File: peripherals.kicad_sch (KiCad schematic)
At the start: 84 parts, among them J14 CONMMCX002-SMD-T, J5 U_FL-R-SMT-1_10_, J7 DM3AT-SF-PEJM5, J8 693022010811, Q13 BSS138-7-F, Q15 BSS138-7-F, Q8 BSS138-7-F, U10 NCP163ASN330T1G

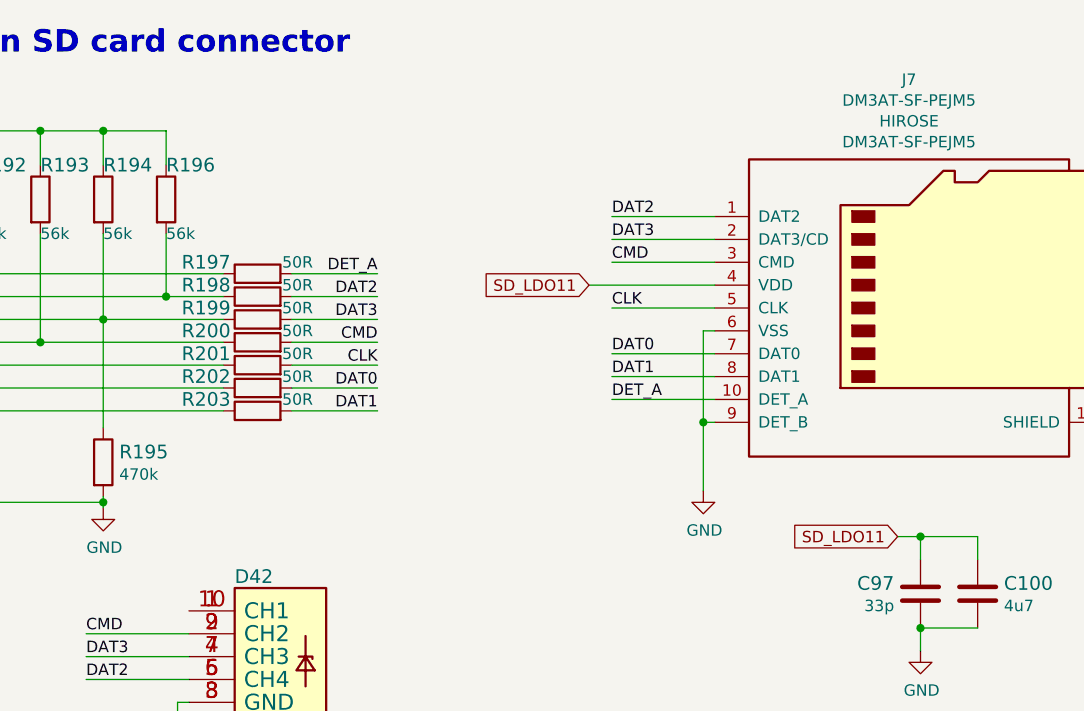
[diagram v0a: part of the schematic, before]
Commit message: Cleared old files. Added 0R after DCDC converters
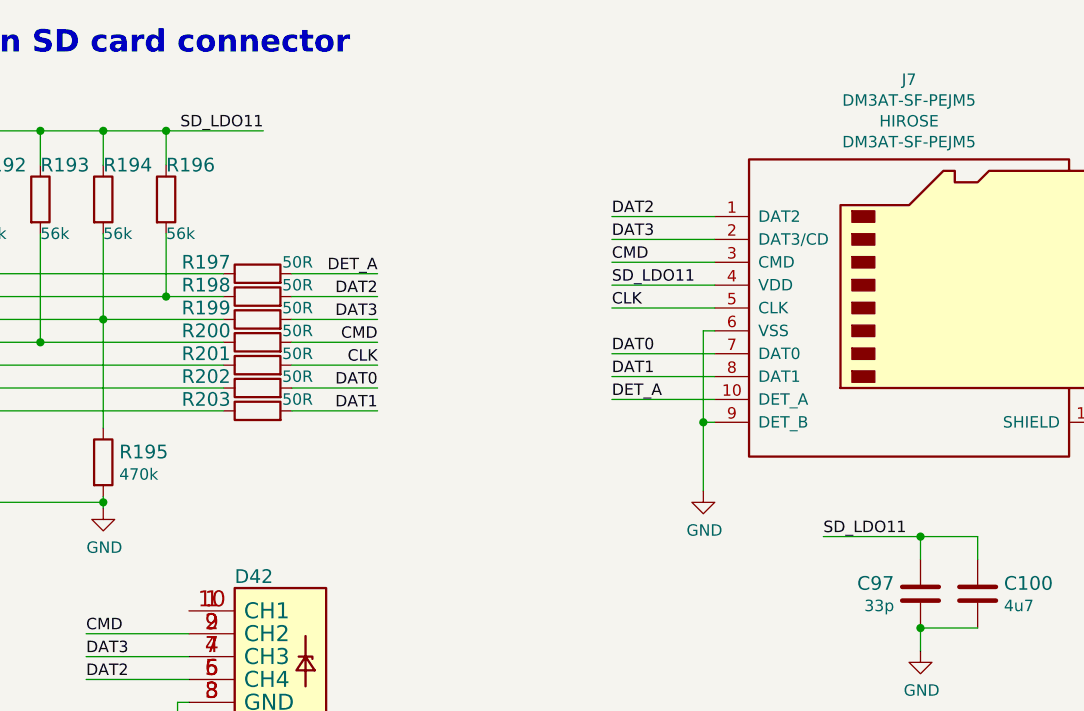
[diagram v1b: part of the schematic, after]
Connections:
- net SD_LDO11 is gone; now on net SD.LDO11: C100.1, C97.1, J7.4 (VDD)

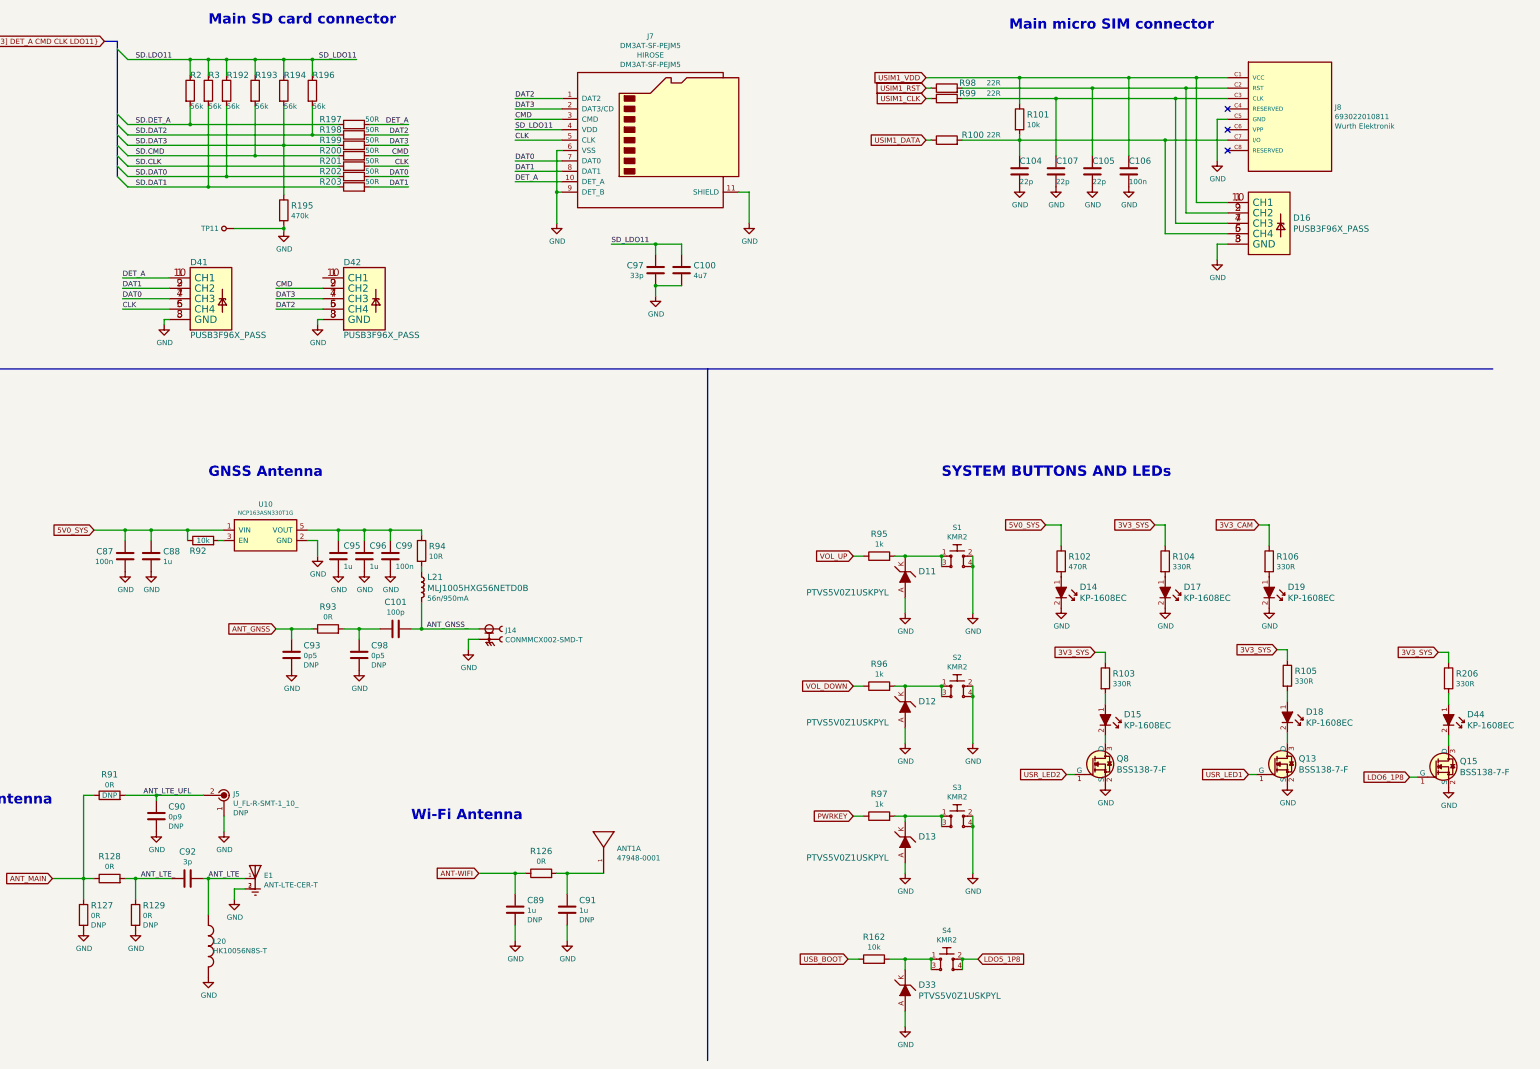
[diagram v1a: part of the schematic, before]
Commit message: Introduce component standardization
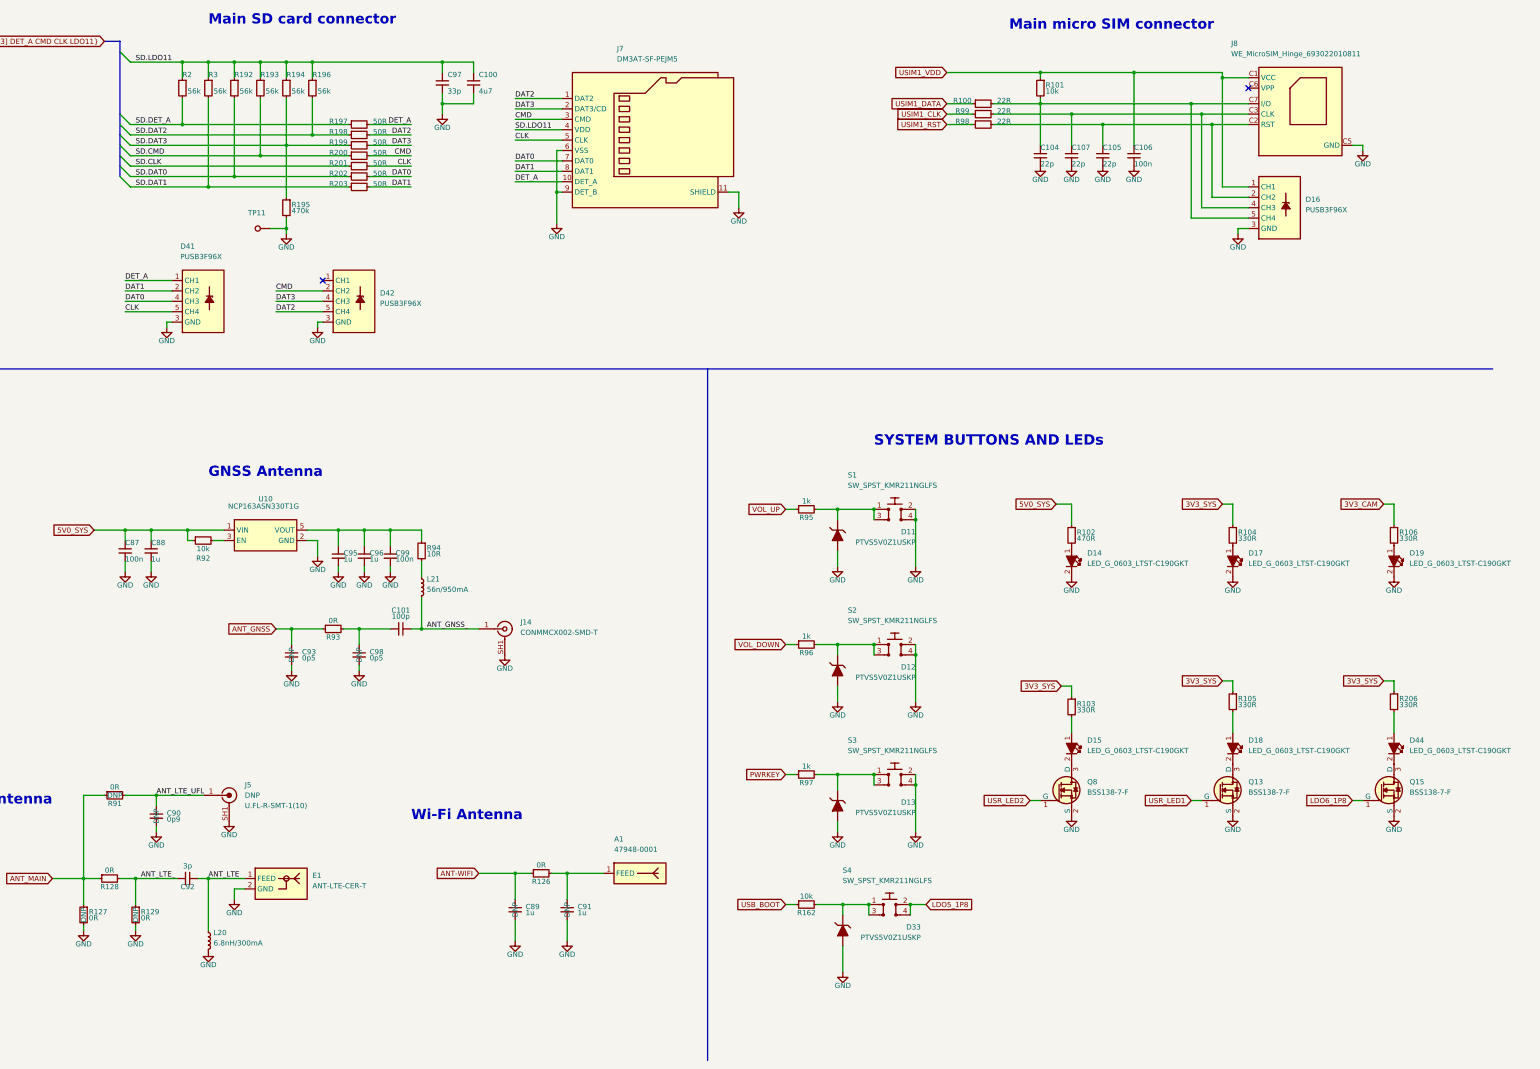
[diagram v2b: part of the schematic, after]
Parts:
- A1: renamed from ANT1; symbol sc606-baseboard:47948-0001-antmicroRFAntennas -> sc606-baseboard:47948-0001; Author (none) -> Antmicro; License (none) -> Apache-2.0
- C100: footprint sc606-baseboard-footprints:0402-cap -> sc606-baseboard-footprints:C_0402_1005Metric; Author (none) -> Antmicro; License (none) -> Apache-2.0; Manufacturer MURATA -> Murata
- C101: footprint sc606-baseboard-footprints:0402-cap -> sc606-baseboard-footprints:C_0402_1005Metric; Author (none) -> Antmicro; Dielectric (none) -> C0G; License (none) -> Apache-2.0; MPN 0402N101J500CT -> GCM1555C1H101JA16D; Manufacturer WALSIN -> Murata; Voltage (none) -> 50V
- C104, C105, C107: footprint sc606-baseboard-footprints:0402-cap -> sc606-baseboard-footprints:C_0402_1005Metric; Author (none) -> Antmicro; License (none) -> Apache-2.0; Manufacturer YAGEO -> Yaego
- C106: footprint sc606-baseboard-footprints:0402-cap -> sc606-baseboard-footprints:C_0402_1005Metric; Author (none) -> Antmicro; Dielectric (none) -> X5R; License (none) -> Apache-2.0; MPN 0402X104K6R3CT -> GRM155R61H104KE14D; Manufacturer Walsin -> Murata; Voltage (none) -> 50V
- C87, C99: footprint sc606-baseboard-footprints:0402-cap -> sc606-baseboard-footprints:C_0402_1005Metric; Author (none) -> Antmicro; Dielectric (none) -> X5R; License (none) -> Apache-2.0; Voltage (none) -> 50V
- C88, C89, C91, C95, C96: footprint sc606-baseboard-footprints:0402-cap -> sc606-baseboard-footprints:C_0402_1005Metric; Author (none) -> Antmicro; License (none) -> Apache-2.0
- C90: footprint sc606-baseboard-footprints:0402-cap -> sc606-baseboard-footprints:C_0402_1005Metric; Author (none) -> Antmicro; License (none) -> Apache-2.0; MPN GJM1555C1HR90DB01D -> GJM1555C1HR90DB01D; Manufacturer MURATA -> Murata
- C92, C97: footprint sc606-baseboard-footprints:0402-cap -> sc606-baseboard-footprints:C_0402_1005Metric; Author (none) -> Antmicro; License (none) -> Apache-2.0; Manufacturer MULTICOMP -> Multicomp
- C93, C98: footprint sc606-baseboard-footprints:0402-cap -> sc606-baseboard-footprints:C_0402_1005Metric; Author (none) -> Antmicro; License (none) -> Apache-2.0; MPN GJM1555C1HR50WB01D -> GJM1555C1HR50WB01D; Manufacturer MURATA -> Murata
- D11, D12, D13, D33: value PTVS5V0Z1USKPYL -> PTVS5V0Z1USKP; symbol sc606-baseboard:PTVS5V0Z1USKPYL -> sc606-baseboard:PTVS5V0Z1USKP; Author (none) -> Antmicro; License (none) -> Apache-2.0
- D14, D15, D17, D18, D19, D44: value KP-1608EC -> LED_G_0603_LTST-C190GKT; footprint sc606-baseboard-footprints:LED_0603 -> sc606-baseboard-footprints:LED_0603_1608Metric_G; symbol sc606-baseboard:KP-1608EC -> sc606-baseboard:LED_G_0603_LTST-C190GKT; Author (none) -> Antmicro; License (none) -> Apache-2.0; MPN KP-1608EC -> LTST-C190GKT; Manufacturer KINGBRIGHT -> Lite-On Inc.
- D16, D41, D42: footprint sc606-baseboard-footprints:PUSB3F96X -> sc606-baseboard-footprints:Nexperia_DFN-10_2.5x1mm_P0.5mm; Author (none) -> Antmicro; License (none) -> Apache-2.0
- E1: footprint sc606-baseboard-footprints:XDCR_ANT-LTE-CER-T -> sc606-baseboard-footprints:Antenna_ANT-LTE-CER-T; Author (none) -> Antmicro; License (none) -> Apache-2.0
- J14: Author (none) -> Antmicro; License (none) -> Apache-2.0; MANUFACTURER Linx Technologies -> (none); Manufacturer (none) -> Linx
- J5: value U_FL-R-SMT-1_10_ -> U_FL-R-SMT-1; symbol sc606-baseboard:U_FL-R-SMT-1_10_ -> sc606-baseboard:U_FL-R-SMT-1; Author (none) -> Antmicro; License (none) -> Apache-2.0; Manufacturer Hirose Electric Co Ltd -> Hirose
- J7: Author (none) -> Antmicro; License (none) -> Apache-2.0; Manufacturer HIROSE -> Hirose
- J8: value 693022010811 -> WE_MicroSIM_Hinge_693022010811; symbol sc606-baseboard:693022010811 -> sc606-baseboard:WE_MicroSIM_Hinge_693022010811; Author (none) -> Antmicro; License (none) -> Apache-2.0; Manufacturer Wurth Elektronik -> Würth Elektronik
- L20: Author (none) -> Antmicro; License (none) -> Apache-2.0; Val (none) -> 6.8nH/300mA
- L21: footprint sc606-baseboard-footprints:0402-res -> sc606-baseboard-footprints:L_0402_1005Metric; Author (none) -> Antmicro; License (none) -> Apache-2.0; MaxCur 950mA -> (none)
- Q13, Q15, Q8: Author (none) -> Antmicro; License (none) -> Apache-2.0
- R100, R98, R99: footprint sc606-baseboard-footprints:0402-res -> sc606-baseboard-footprints:R_0402_1005Metric; Author (none) -> Antmicro; License (none) -> Apache-2.0; MPN CRCW040222R0FKED -> CR0402-FX-22R0GLF; Manufacturer VISHAY -> Bourns; Tolerance (none) -> 1%
- R101, R162, R92: footprint sc606-baseboard-footprints:0402-res -> sc606-baseboard-footprints:R_0402_1005Metric; Author (none) -> Antmicro; License (none) -> Apache-2.0; MPN CRCW040210K0FKEDHP -> CR0402-FX-1002GLF; Manufacturer VISHAY -> Bourns; Tolerance (none) -> 1%
- R102: footprint sc606-baseboard-footprints:0402-res -> sc606-baseboard-footprints:R_0402_1005Metric; Author (none) -> Antmicro; License (none) -> Apache-2.0; MPN CRCW0402470RFKED -> CR0402-FX-4700GLF; Manufacturer VISHAY -> Bourns; Tolerance (none) -> 1%
- R103, R104, R105, R106, R206: footprint sc606-baseboard-footprints:0402-res -> sc606-baseboard-footprints:R_0402_1005Metric; Author (none) -> Antmicro; License (none) -> Apache-2.0; MPN MCMR04X3300FTL -> CR0402-FX-3300GLF; Manufacturer MULTICOMP -> Bourns; Tolerance (none) -> 1%
- R126, R127, R128, R129, R91, R93: footprint sc606-baseboard-footprints:0402-res -> sc606-baseboard-footprints:R_0402_1005Metric; Author (none) -> Antmicro; Current (none) -> 1A; License (none) -> Apache-2.0; Manufacturer PANASONIC -> Panasonic
- R192, R193, R194, R196, R2, R3: footprint sc606-baseboard-footprints:0402-res -> sc606-baseboard-footprints:R_0402_1005Metric; Author (none) -> Antmicro; License (none) -> Apache-2.0; MPN CRCW040256K0FKED -> CR0402-FX-5602GLF; Manufacturer VISHAY -> Bourns; Tolerance (none) -> 1%
- R195: footprint antmicro-footprints:0402-res -> sc606-baseboard-footprints:R_0402_1005Metric; symbol antmicroResistors0402:R_470k_0402 -> sc606-baseboard:R_470k_0402; Author (none) -> Antmicro; License (none) -> Apache-2.0; MPN RC0402FR-07470KL -> CR0402-FX-4703GLF; Manufacturer YAGEO -> Bourns; Tolerance (none) -> 1%
- R197, R198, R199, R200, R201, R202, R203: footprint sc606-baseboard-footprints:0402-res -> sc606-baseboard-footprints:R_0402_1005Metric; Author (none) -> Antmicro; License (none) -> Apache-2.0; MPN RN73R1ETTP50R0F50 -> CR0402-FX-50R0GLF; Manufacturer KOA -> Bourns; Tolerance (none) -> 1%
- R94: footprint sc606-baseboard-footprints:0603-res -> sc606-baseboard-footprints:R_0603_1608Metric; Author (none) -> Antmicro; License (none) -> Apache-2.0; MPN MCWR06X10R0FTL -> CR0603-FX-10R0ELF; Manufacturer MULTICOMP -> Bourns; Tolerance (none) -> 1%
- R95, R96, R97: footprint sc606-baseboard-footprints:0402-res -> sc606-baseboard-footprints:R_0402_1005Metric; Author (none) -> Antmicro; License (none) -> Apache-2.0; Manufacturer BOURNS -> Bourns; Tolerance (none) -> 1%
- S1, S2, S3, S4: value KMR2 -> SW_SPST_KMR211NGLFS; symbol sc606-baseboard:KMR2 -> sc606-baseboard:SW_SPST_KMR211NGLFS; Author (none) -> Antmicro; License (none) -> Apache-2.0; Manufacturer C&K Components -> C&K
- TP11: value TP_SMD_1_5MM -> TP_1.5mm_SMD; footprint sc606-baseboard-footprints:TP-R-1.5 -> sc606-baseboard-footprints:TP_SMD_1.5mm; symbol sc606-baseboard:TP_SMD_0_75MM -> sc606-baseboard:TP_1.5mm_SMD; Author (none) -> Antmicro; License (none) -> Apache-2.0
- U10: Author (none) -> Antmicro; License (none) -> Apache-2.0; Manufacturer Onsemi -> ON Semiconductor
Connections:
- net ANT_LTE_UFL: now also J5.1; no longer J5.2
- net GND: now also J14.SH1, J14.SH2, J14.SH3, J14.SH4, J5.SH1, J5.SH2; no longer J14.S1, J14.S2, J14.S3, J14.S4, J5.1
- no-connect marks 3 -> 2
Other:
- moved on the sheet: C100, C101, C104, C105, C106, C107, C87, C88, C89, C90, C91, C92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

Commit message: [#61796] Run globlib
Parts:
- A1: footprint sc606-baseboard-footprints:47948-0001 -> antmicro-footprints:47948-0001; symbol sc606-baseboard:47948-0001 -> antmicroRFAntennas:47948-0001
- C100: footprint sc606-baseboard-footprints:C_0402_1005Metric -> antmicro-footprints:C_0402_1005Metric; symbol sc606-baseboard:C_4u7_0402 -> antmicroCapacitors0402:C_4u7_0402
- C101: footprint sc606-baseboard-footprints:C_0402_1005Metric -> antmicro-footprints:C_0402_1005Metric; symbol sc606-baseboard:C_100p_0402 -> antmicroCapacitors0402:C_100p_0402
- C104, C105, C107: footprint sc606-baseboard-footprints:C_0402_1005Metric -> antmicro-footprints:C_0402_1005Metric; symbol sc606-baseboard:C_22p_0402 -> antmicroCapacitors0402:C_22p_0402
- C106, C87, C99: footprint sc606-baseboard-footprints:C_0402_1005Metric -> antmicro-footprints:C_0402_1005Metric; symbol sc606-baseboard:C_100n_0402 -> antmicroCapacitors0402:C_100n_0402
- C88, C89, C91, C95, C96: footprint sc606-baseboard-footprints:C_0402_1005Metric -> antmicro-footprints:C_0402_1005Metric; symbol sc606-baseboard:C_1u_0402 -> antmicroCapacitors0402:C_1u_0402
- C90: footprint sc606-baseboard-footprints:C_0402_1005Metric -> antmicro-footprints:C_0402_1005Metric; symbol sc606-baseboard:C_0p9_0402 -> antmicroCapacitors0402:C_0p9_0402
- C92: footprint sc606-baseboard-footprints:C_0402_1005Metric -> antmicro-footprints:C_0402_1005Metric; symbol sc606-baseboard:C_3p_0402 -> antmicroCapacitors0402:C_3p_0402
- C93, C98: footprint sc606-baseboard-footprints:C_0402_1005Metric -> antmicro-footprints:C_0402_1005Metric; symbol sc606-baseboard:C_0p5_0402 -> antmicroCapacitors0402:C_0p5_0402
- C97: footprint sc606-baseboard-footprints:C_0402_1005Metric -> antmicro-footprints:C_0402_1005Metric; symbol sc606-baseboard:C_33p_0402 -> antmicroCapacitors0402:C_33p_0402
- D11, D12, D13, D33: footprint sc606-baseboard-footprints:SOD-964 -> antmicro-footprints:D_SOD-964; symbol sc606-baseboard:PTVS5V0Z1USKP -> antmicroTVSDiodes:PTVS5V0Z1USKP
- D14, D15, D17, D18, D19, D44: footprint sc606-baseboard-footprints:LED_0603_1608Metric_G -> antmicro-footprints:LED_0603_1608Metric_G; symbol sc606-baseboard:LED_G_0603_LTST-C190GKT -> antmicroLEDIndicationDiscrete:LED_G_0603_LTST-C190GKT
- D16, D41, D42: footprint sc606-baseboard-footprints:Nexperia_DFN-10_2.5x1mm_P0.5mm -> antmicro-footprints:Nexperia_DFN-10_2.5x1mm_P0.5mm; symbol sc606-baseboard:PUSB3F96X_PASS -> antmicroTVSDiodes:PUSB3F96X_PASS
- E1: footprint sc606-baseboard-footprints:Antenna_ANT-LTE-CER-T -> antmicro-footprints:Antenna_ANT-LTE-CER-T; symbol sc606-baseboard:ANT-LTE-CER-T -> antmicroRFAntennas:ANT-LTE-CER-T
- J14: footprint sc606-baseboard-footprints:LINX_CONMMCX002-SMD-T -> antmicro-footprints:LINX_CONMMCX002-SMD-T; symbol sc606-baseboard:CONMMCX002-SMD-T -> antmicroCoaxialConnectorsRF:CONMMCX002-SMD-T
- J5: footprint sc606-baseboard-footprints:Coax_Conn_U.FL -> antmicro-footprints:Coax_Conn_U.FL; symbol sc606-baseboard:U_FL-R-SMT-1 -> antmicroCoaxialConnectorsRF:U_FL-R-SMT-1
- J7: footprint sc606-baseboard-footprints:MicroSD_DM3AT-SF-PEJM5 -> antmicro-footprints:MicroSD_DM3AT-SF-PEJM5; symbol sc606-baseboard:DM3AT-SF-PEJM5 -> antmicroMemoryConnectorsPCCardSockets:DM3AT-SF-PEJM5
- J8: footprint sc606-baseboard-footprints:693022010811 -> antmicro-footprints:693022010811; symbol sc606-baseboard:WE_MicroSIM_Hinge_693022010811 -> antmicroSimCardConnectors:WE_MicroSIM_Hinge_693022010811
- L21: footprint sc606-baseboard-footprints:L_0402_1005Metric -> antmicro-footprints:L_0402_1005Metric; symbol sc606-baseboard:MLJ1005HXG56NETD0B -> antmicroFixedInductors:L_56n_0.95A_0402
- Q13, Q15, Q8: footprint sc606-baseboard-footprints:SOT-23-3 -> antmicro-footprints:SOT-23-3; symbol sc606-baseboard:BSS138-7-F -> antmicroTransistorsFETsMOSFETsSingle:BSS138-7-F
- R100, R98, R99: footprint sc606-baseboard-footprints:R_0402_1005Metric -> antmicro-footprints:R_0402_1005Metric; symbol sc606-baseboard:R_22R_0402 -> antmicroResistors0402:R_22R_0402
- R101, R162, R92: footprint sc606-baseboard-footprints:R_0402_1005Metric -> antmicro-footprints:R_0402_1005Metric; symbol sc606-baseboard:R_10k_0402 -> antmicroResistors0402:R_10k_0402
- R102: footprint sc606-baseboard-footprints:R_0402_1005Metric -> antmicro-footprints:R_0402_1005Metric; symbol sc606-baseboard:R_470R_0402 -> antmicroResistors0402:R_470R_0402
- R103, R104, R105, R106, R206: footprint sc606-baseboard-footprints:R_0402_1005Metric -> antmicro-footprints:R_0402_1005Metric; symbol sc606-baseboard:R_330R_0402 -> antmicroResistors0402:R_330R_0402
- R126, R127, R128, R129, R91, R93: footprint sc606-baseboard-footprints:R_0402_1005Metric -> antmicro-footprints:R_0402_1005Metric; symbol sc606-baseboard:R_0R_0402 -> antmicroResistors0402:R_0R_0402
- R192, R193, R194, R196, R2, R3: footprint sc606-baseboard-footprints:R_0402_1005Metric -> antmicro-footprints:R_0402_1005Metric; symbol sc606-baseboard:R_56k_0402 -> antmicroResistors0402:R_56k_0402
- R195: footprint sc606-baseboard-footprints:R_0402_1005Metric -> antmicro-footprints:R_0402_1005Metric; symbol sc606-baseboard:R_470k_0402 -> antmicroResistors0402:R_470k_0402
- R197, R198, R199, R200, R201, R202, R203: footprint sc606-baseboard-footprints:R_0402_1005Metric -> antmicro-footprints:R_0402_1005Metric; symbol sc606-baseboard:R_50R_0402 -> antmicroResistors0402:R_50R_0402
- R94: footprint sc606-baseboard-footprints:R_0603_1608Metric -> antmicro-footprints:R_0603_1608Metric; symbol sc606-baseboard:R_10R_0603 -> antmicroResistors0603:R_10R_0603
- R95, R96, R97: footprint sc606-baseboard-footprints:R_0402_1005Metric -> antmicro-footprints:R_0402_1005Metric; symbol sc606-baseboard:R_1k_0402 -> antmicroResistors0402:R_1k_0402
- S1, S2, S3, S4: footprint sc606-baseboard-footprints:SW_SPST_4.2x2.8 -> antmicro-footprints:SW_KMR211NGLFS_SMD; symbol sc606-baseboard:SW_SPST_KMR211NGLFS -> antmicroPushbuttonSwitches:SW_KMR211NGLFS_SMD
- TP11: footprint sc606-baseboard-footprints:TP_SMD_1.5mm -> antmicro-footprints:TP_SMD_1.5mm; symbol sc606-baseboard:TP_1.5mm_SMD -> antmicroTestPoints:TP_1.5mm_SMD
- U10: footprint sc606-baseboard-footprints:SOT-23-5 -> antmicro-footprints:SOT-23-5; symbol sc606-baseboard:NCP163ASN330T1G -> antmicroPMICVoltageRegulatorsLinear:NCP163ASN330T1G
